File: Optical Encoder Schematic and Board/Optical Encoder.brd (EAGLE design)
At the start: 58.1 x 43.2 mm, 30 parts, among them U1 ATMEGA328P, Y1 16MHz

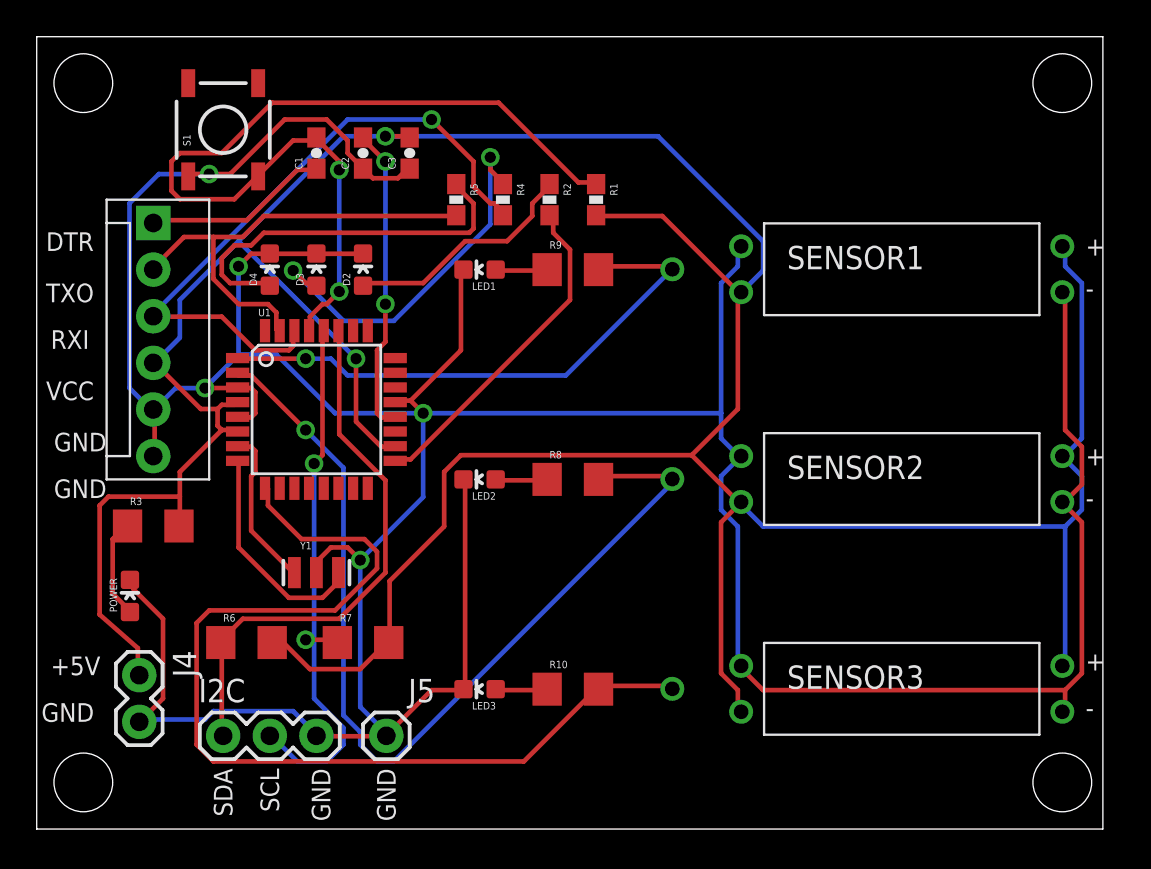
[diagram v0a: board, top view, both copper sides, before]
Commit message: Updated Optical encoder board with latest changes. Added 2 status LEDs to ICSP board.
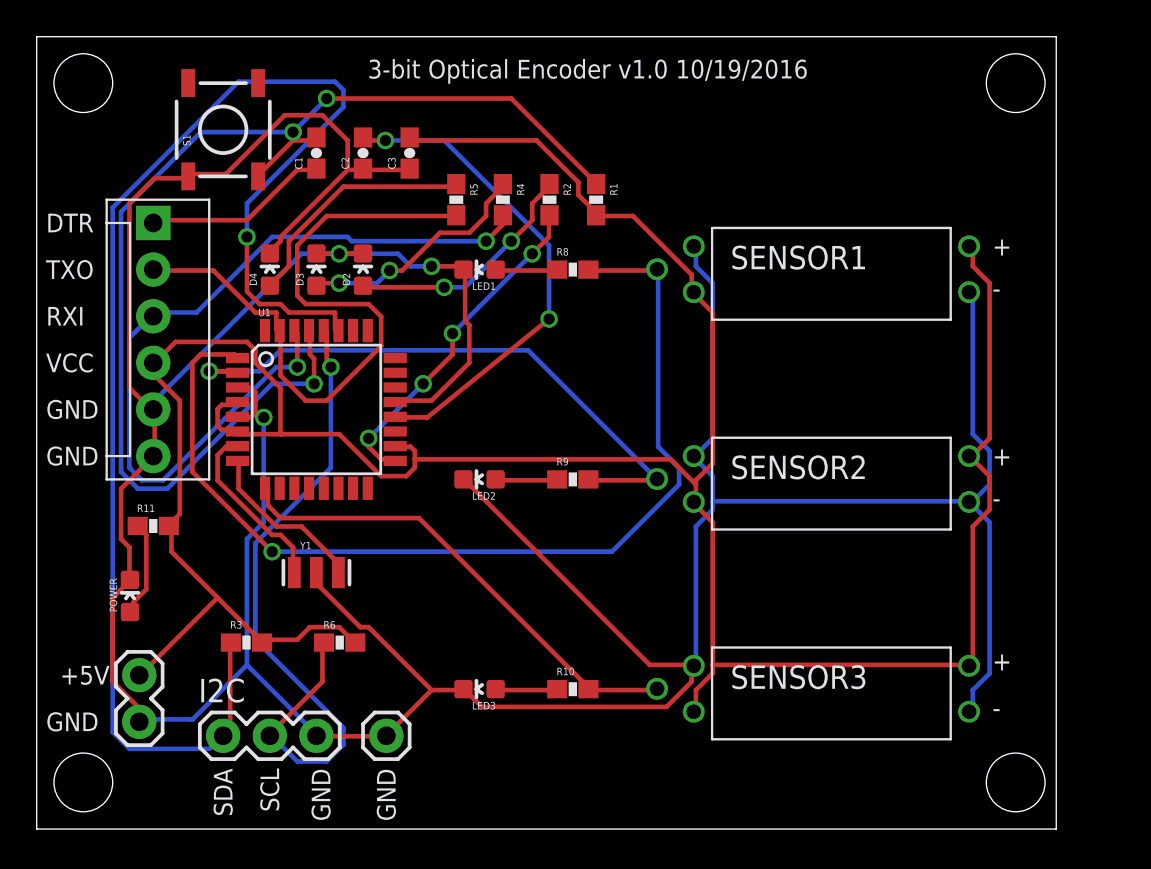
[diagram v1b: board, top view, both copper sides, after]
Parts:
- removed R7: 4.7k, SparkFun-Resistors:1206
- added R11: 150, SparkFun-Passives:0603-RES
- R10, R6, R8, R9: device SparkFun-Resistors:1206 -> SparkFun-Passives:0603-RES
- R3: value 150 -> 4.7k; device SparkFun-Resistors:1206 -> SparkFun-Passives:0603-RES
- moved R8 11.4 mm to (26.7, 27.9)
- moved R9 11.4 mm to (26.7, 16.5)
- moved R3 8.13 mm to (8.89, 7.62)
- moved SENSOR1 5.08 mm to (48.3, 29.2)
- moved SENSOR2 5.08 mm to (48.3, 17.8)
- moved SENSOR3 5.08 mm to (48.3, 6.35)
- moved R6 5.08 mm to (14.0, 7.62)
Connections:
- net D3: now also R8.2; no longer R9.2
- net D4: now also R9.2; no longer R8.2
- net N$20: now also R9.1; no longer R8.1
- net N$7: now also R8.1; no longer R9.1
- net N$9: now also R11.1; no longer R3.1
- net SCL: now also R6.1; no longer R7.1
- net SDA: now also R3.1; no longer R6.1
- net VCC: now also R11.2; no longer R7.2
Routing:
- net SDA: track 29.9 -> 75.6 mm, vias 0 -> 1
- net VCC: track 201.2 -> 157.1 mm, vias 2 -> 0
- net D5: track 54.8 -> 26.5 mm
- net D3: track 30.7 -> 54.5 mm
- net D4: track 51.7 -> 33.1 mm
- net RESET: track 49.3 -> 65.4 mm, vias 2 -> 3
- net TXO: track 25.4 -> 37.2 mm
- net AREF: track 16.8 -> 26.9 mm
- net RXI: track 36.0 -> 44.8 mm, vias 1 -> 2
- net N$5: track 21.1 -> 13.0 mm
- net N$6: track 21.0 -> 13.2 mm
- net GND: track 226.5 -> 233.6 mm, vias 5 -> 3
- net SCL: track 30.6 -> 37.7 mm, vias 2 -> 1
- net N$2: track 12.3 -> 9.26 mm
- net N$1: track 8.81 -> 9.73 mm
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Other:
- board size 58.1 x 43.2 mm -> 55.5 x 43.2 mm
- board text added: "3-bit Optical Encoder v1.0 10/19/2016"
